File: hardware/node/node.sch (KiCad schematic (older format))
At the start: 64 parts, among them J1 BOOT0_Jumper, J2 FTDI, J3 SMA Female, J4 2 x AA, J5 SWD, Q1 Si2323DDS, SW1 TVCM04N016BB, U1 RFM69HW, U2 SHTC3, U3 AT25DF512C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

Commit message: Changed switch
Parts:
- J2: footprint Connector_PinHeader_2.54mm:PinHeader_1x06_P2.54mm_Vertical -> Connector_PinHeader_2.54mm:PinHeader_1x06_P2.54mm_Horizontal
- SW1: value TVCM04N016BB -> DTSM-65R-V-B; footprint humidity:SW_TVCM04-N -> humidity:SW_SPST_DTSM-6
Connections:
- net STM_RESET: now also SW1.2; no longer SW1.1
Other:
- moved on the sheet: SW1
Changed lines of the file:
@@
 L power:GND #PWR032
 U 1 1 5CE4C513
-P 11000 3150
-F 0 "#PWR032" H 11000 2900 50  0001 C CNN
-F 1 "GND" H 11005 2977 50  0000 C CNN
-F 2 "" H 11000 3150 50  0001 C CNN
-F 3 "" H 11000 3150 50  0001 C CNN
-	1    11000 3150
-	1    0    0    -1
-$EndComp
-Wire Wire Line
-	10900 2650 11000 2650
-Wire Wire Line
-	11000 2650 11000 3150
+P 11000 3050
+F 0 "#PWR032" H 11000 2800 50  0001 C CNN
+F 1 "GND" H 11005 2877 50  0000 C CNN
+F 2 "" H 11000 3050 50  0001 C CNN
+F 3 "" H 11000 3050 50  0001 C CNN
+	1    11000 3050
+	1    0    0    -1
+$EndComp
+Wire Wire Line
+	10900 2550 11000 2550
+Wire Wire Line
+	11000 2550 11000 3050
 $Comp
 L Device:LED D2
@@
 F 0 "J2" H 4700 5100 50  0000 R CNN
 F 1 "FTDI" H 4700 4350 50  0000 C CNN
-F 2 "Connector_PinHeader_2.54mm:PinHeader_1x06_P2.54mm_Vertical" H 4600 4800 50  0001 C CNN
+F 2 "Connector_PinHeader_2.54mm:PinHeader_1x06_P2.54mm_Horizontal" H 4600 4800 50  0001 C CNN
 F 3 "~" H 4600 4800 50  0001 C CNN
 	1    4600 4800
@@
 L humidity:SW_Push_4pin SW1
 U 1 1 5DEFB807
-P 10650 2650
-F 0 "SW1" H 10750 2800 40  0000 C CNN
-F 1 "TVCM04N016BB" H 10650 2450 40  0000 C CNN
-F 2 "humidity:SW_TVCM04-N" H 10650 2650 40  0001 C CNN
-F 3 "https://www.tme.eu/Document/1590b299897e66d73e44ecd41b5c73b5/TVCM04N016BB.jpg" H 10650 2650 40  0001 C CNN
-	1    10650 2650
-	1    0    0    -1
-$EndComp
-NoConn ~ 10900 2750
-NoConn ~ 10400 2750
+P 10650 2550
+F 0 "SW1" H 10750 2700 40  0000 C CNN
+F 1 "DTSM-65R-V-B" H 10650 2350 40  0000 C CNN
+F 2 "humidity:SW_SPST_DTSM-6" H 10650 2550 40  0001 C CNN
+F 3 "https://www.tme.eu/se/en/details/dtsm-65r-v-b/microswitches-tact/diptronics/" H 10650 2550 40  0001 C CNN
+	1    10650 2550
+	1    0    0    -1
+$EndComp
+NoConn ~ 10900 2650
+NoConn ~ 10400 2550
 Text Notes 4100 7700 0    40   ~ 0
 Vary duty cycle linearly  depending\non VCC to get constant luminosity

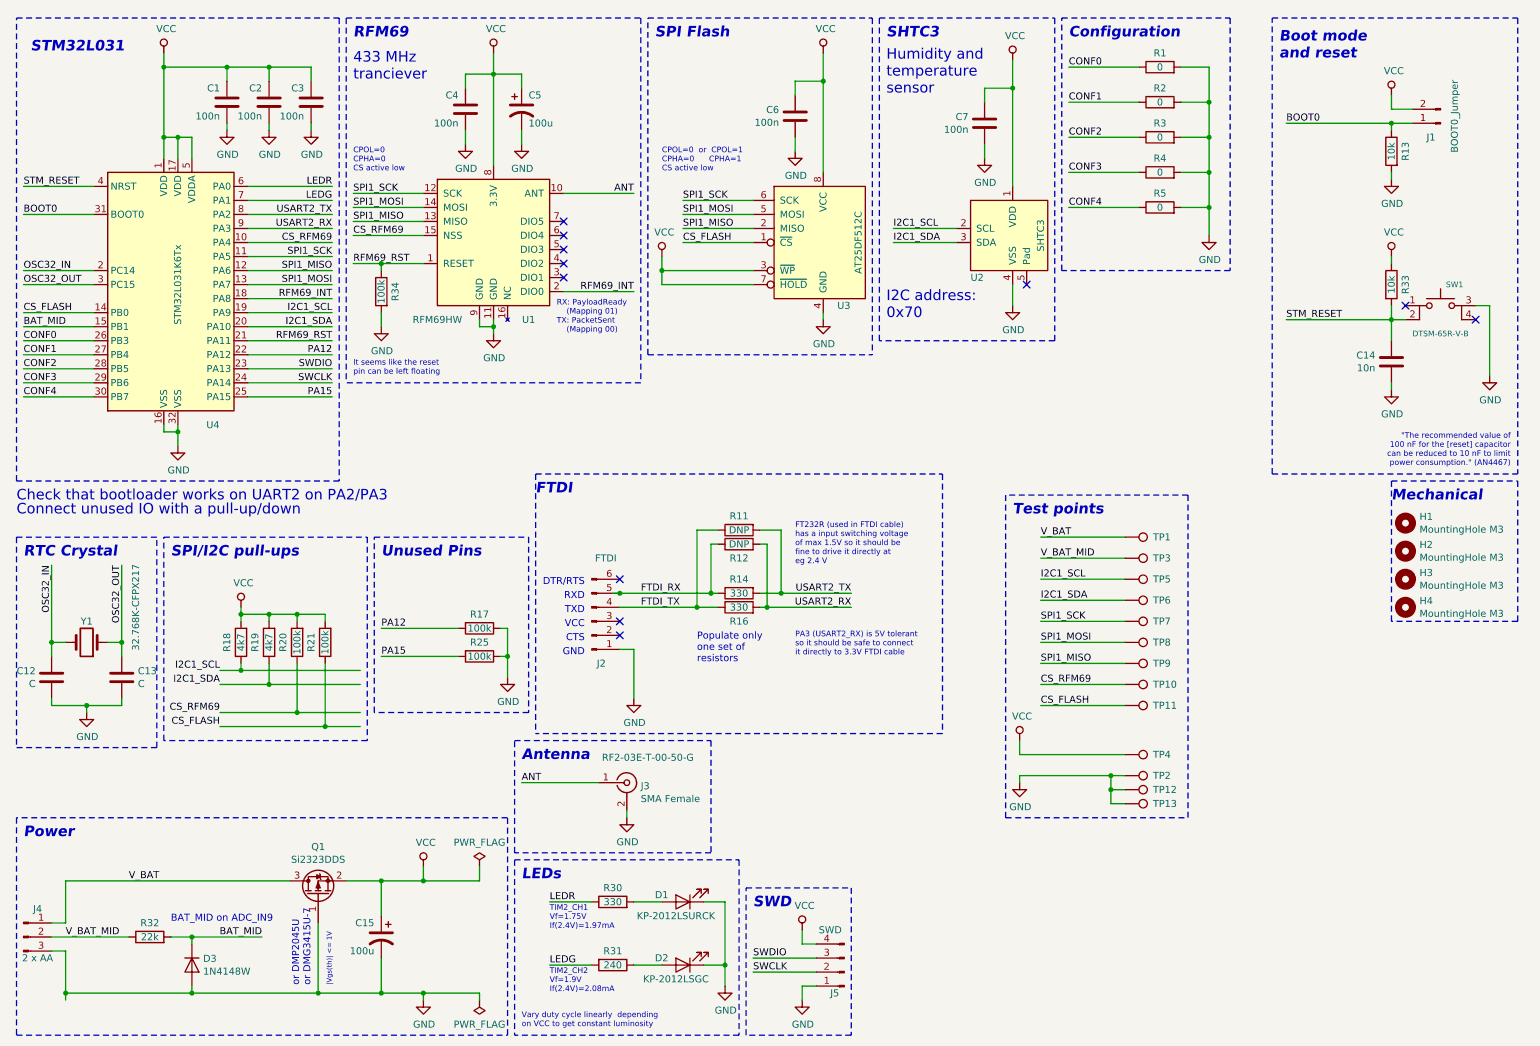
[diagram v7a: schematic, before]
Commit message: Added part numbers to node schematic
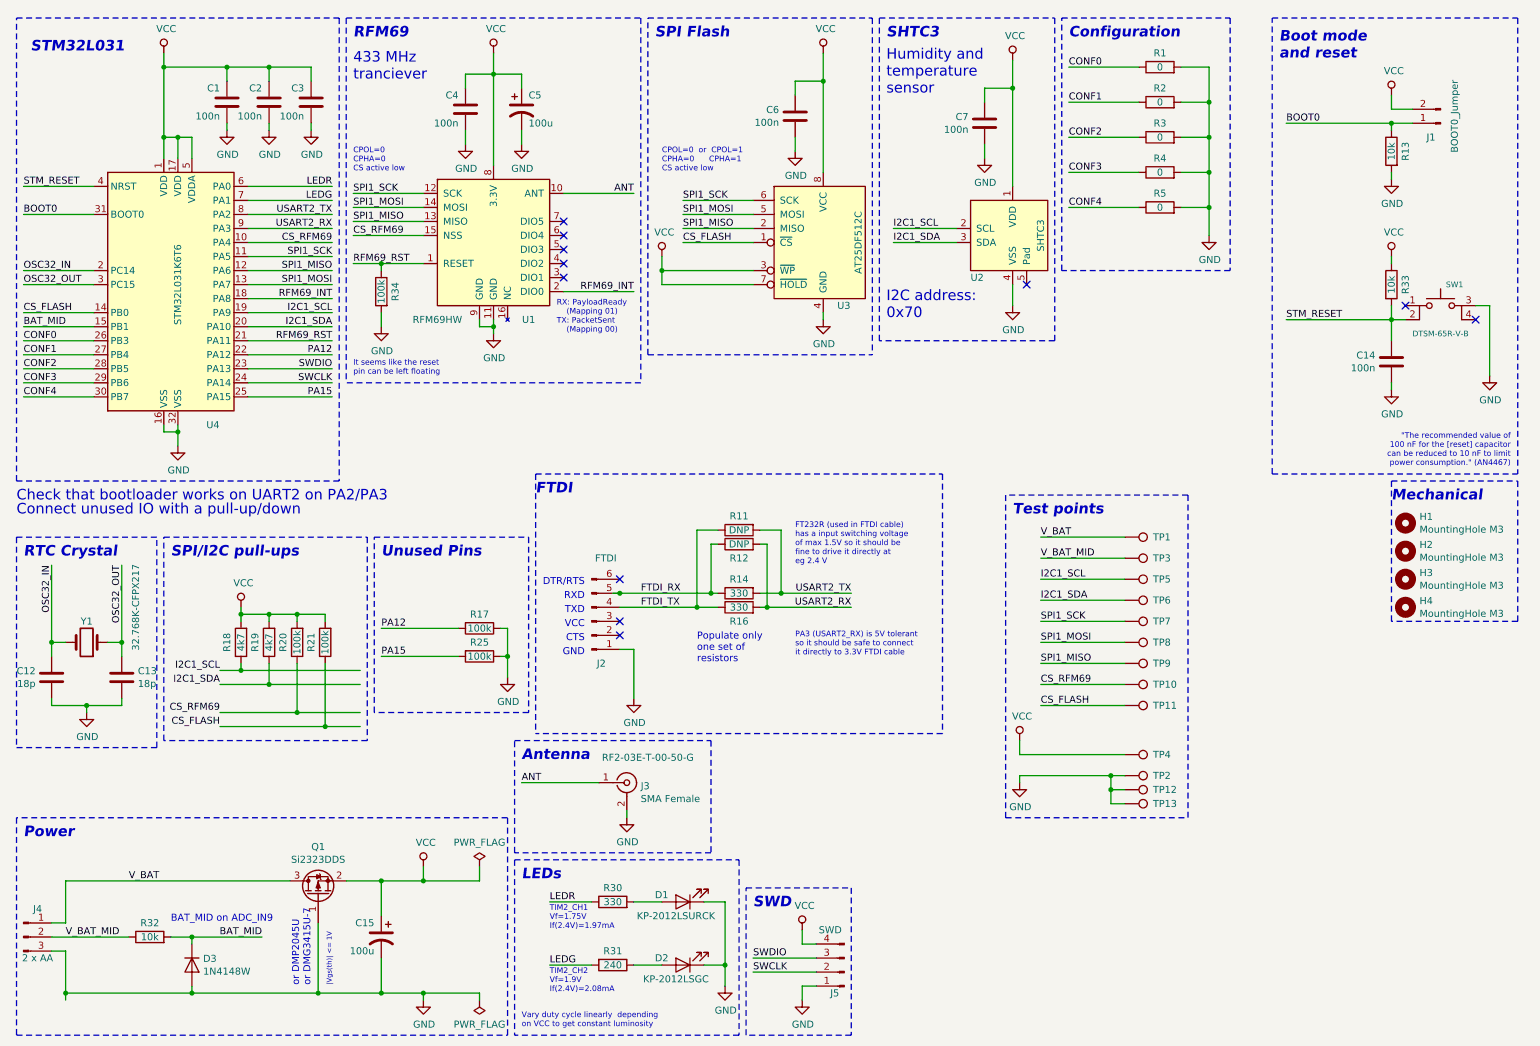
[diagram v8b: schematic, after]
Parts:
- C1, C2, C3, C4, C6, C7: TME Link (none) -> https://www.tme.eu/se/en/details/cl10b104ko8nnnc/0603-mlcc-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; TME Price (none) -> 0.13310
- C12, C13: value C -> 18p; TME Link (none) -> https://www.tme.eu/se/en/details/vj0603a180jxacw2bc/0603-ml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; TME Price (none) -> 0.13033
- C14: value 10n -> 100n; TME Link (none) -> https://www.tme.eu/se/en/details/cl10b104ko8nnnc/0603-mlcc-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; TME Price (none) -> 0.13310
- C15, C5: TME Link (none) -> https://www.tme.eu/se/en/details/sc1c107m6l005vr/85degc-smd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; TME Price (none) -> 0.35458
- D1: TME Link (none) -> https://www.tme.eu/se/en/details/kp-2012lsurck/smd-colour-l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; TME Price (none) -> 1.0254
- D2: TME Link (none) -> https://www.tme.eu/se/en/details/kp-2012lsgc/smd-colour-led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; TME Price (none) -> 1.0520
- D3: TME Link (none) -> https://www.tme.eu/se/en/details/1n4148w-7-f/smd-universal-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; TME Price (none) -> 0.2481
- H1, H2, H3, H4, R11, R12, TP1, TP10, TP11, TP12, TP13, TP2, TP3, TP4, TP5, TP6, TP7, TP8, TP9: TME Link (none) -> -
- J3: TME Link (none) -> https://www.tme.eu/se/en/details/rf2-03e-t-00-50-g/sma-smb-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; TME Price (none) -> 12.76
- J4: TME Link (none) -> https://www.tme.eu/se/en/details/zl262-3sg/pin-headers/conn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; TME Price (none) -> 0.60822
- Q1: TME Link (none) -> https://www.tme.eu/se/en/details/si2323dds-t1-ge3/smd-p-cha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; TME Price (none) -> 3.34344
- R1, R2, R3, R4, R5: TME Link (none) -> https://www.tme.eu/se/en/details/smd0603-0r/0603-smd-resist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; TME Price (none) -> 0.09735
- R13, R33: TME Link (none) -> https://www.tme.eu/se/en/details/crcw060310k0fktabc/0603-sm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; TME Price (none) -> 0.12458
- R14, R16, R30: TME Link (none) -> https://www.tme.eu/se/en/details/smd0603-330r-1%25/0603-smd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; TME Price (none) -> 0.11531
- R17, R20, R21, R25, R34: TME Link (none) -> https://www.tme.eu/se/en/details/cq0603-100k-1%25/0603-smd-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; TME Price (none) -> 0.18525
- R18, R19: TME Link (none) -> https://www.tme.eu/se/en/details/smd0603-4k7-1%25/0603-smd-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; TME Price (none) -> 0.115131
- R31: TME Link (none) -> https://www.tme.eu/se/en/details/smd0603-240r-1%25/0603-smd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; TME Price (none) -> 0.11531
- R32: value 22k -> 10k; TME Link (none) -> https://www.tme.eu/se/en/details/crcw060310k0fktabc/0603-sm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; TME Price (none) -> 0.12458
- SW1: TME Link (none) -> https://www.tme.eu/se/en/details/dtsm-65r-v-b/microswitches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; TME Price (none) -> 1.8894
- U1: TME Link (none) -> https://www.tme.eu/se/en/details/rfm69hw-433s2/rf-modules/h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; TME Price (none) -> 29.96
- U2: TME Link (none) -> https://www.tme.eu/se/en/details/shtc3/humidity-sensors/sen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; TME Price (none) -> 16.93
- U3: TME Link (none) -> https://www.tme.eu/se/en/details/at25df512c-sshngub/serial-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; TME Price (none) -> 4.54
- U4: value STM32L031K6Tx -> STM32L031K6T6; TME Link (none) -> https://www.tme.eu/se/en/details/stm32l031k6t6/st-microcont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; TME Price (none) -> 20.98
- Y1: TME Link (none) -> https://www.tme.eu/se/en/details/32.768k-cfpx217/smd-quartz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; TME Price (none) -> 3.42863
